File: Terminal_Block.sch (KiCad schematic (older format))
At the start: 0 parts

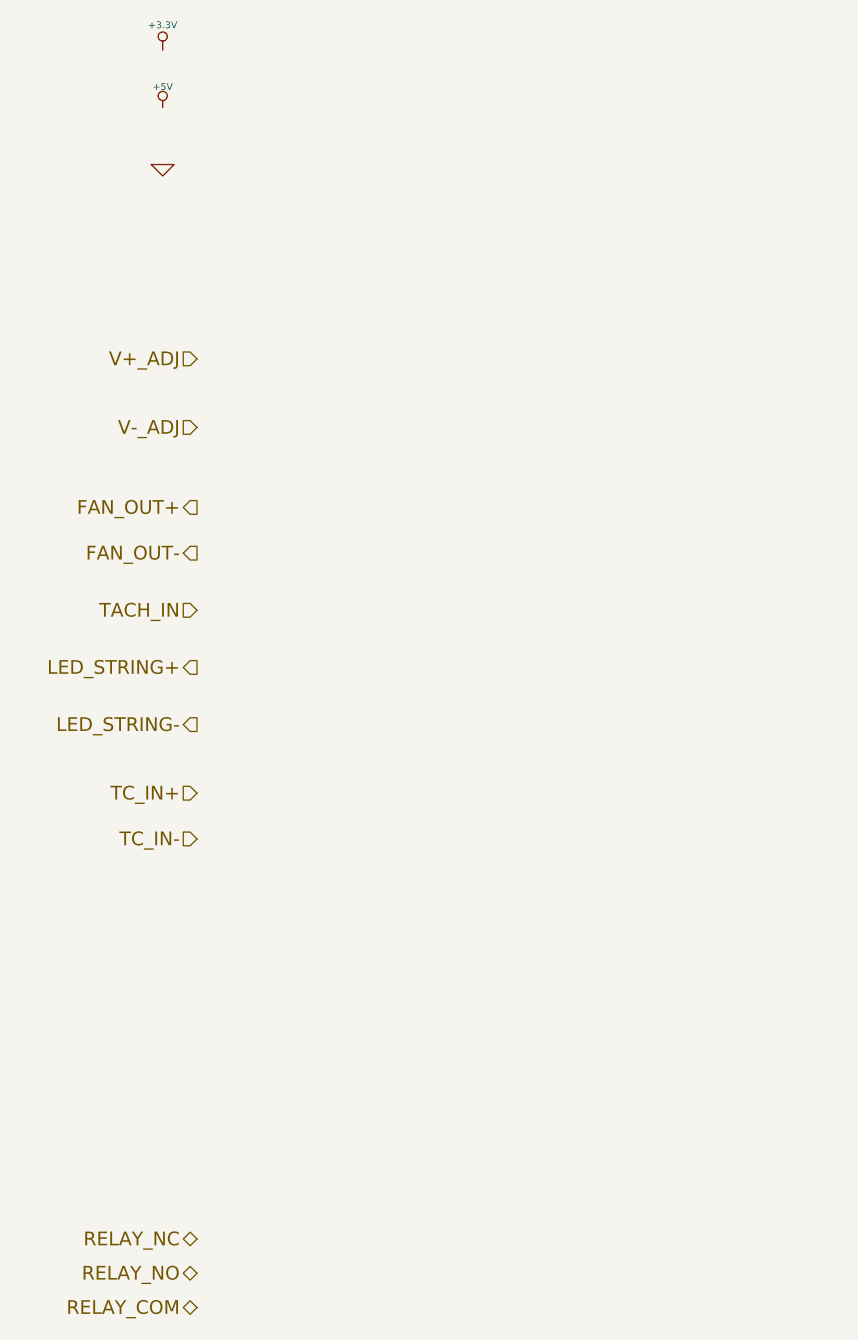
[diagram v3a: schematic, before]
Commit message: Added Arduino Connect Pin Layout
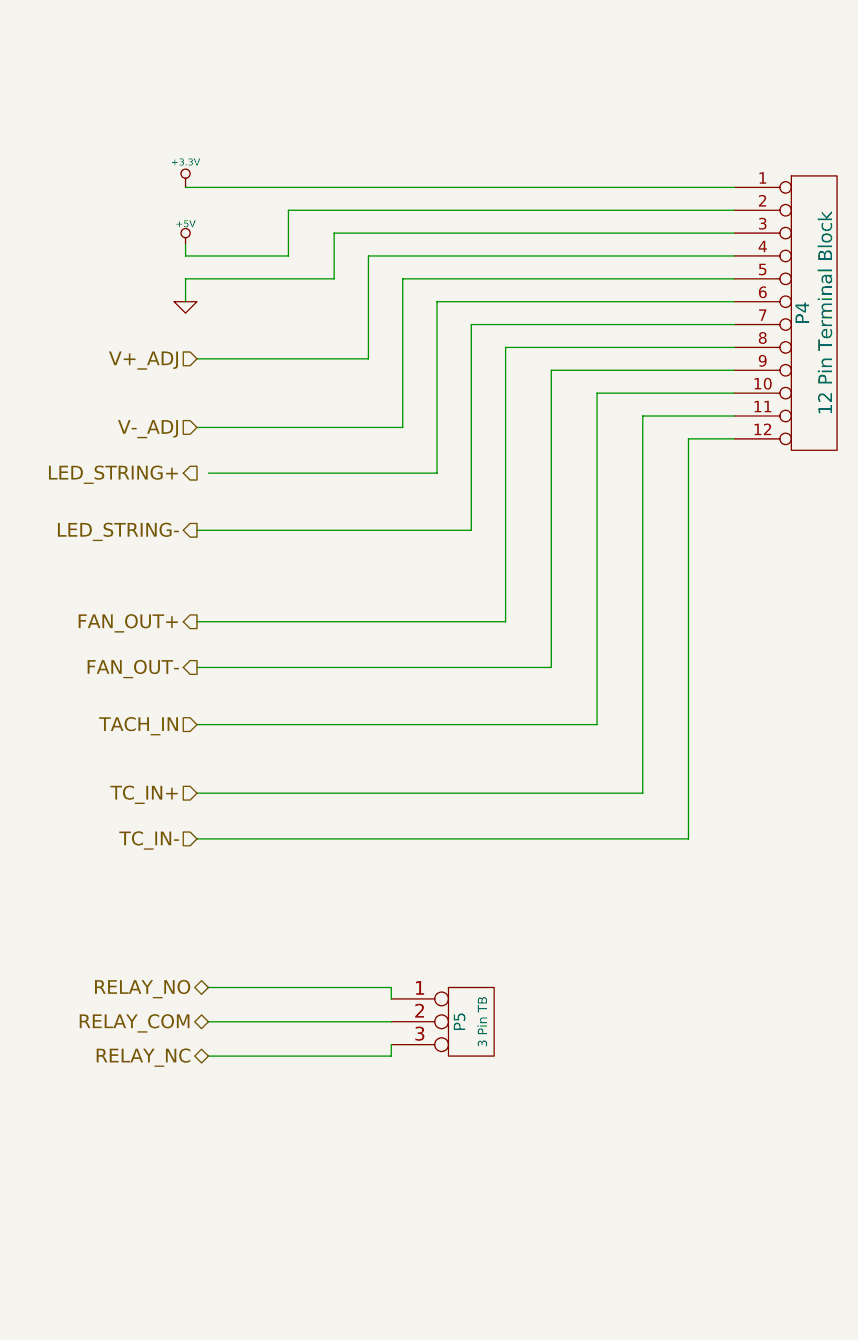
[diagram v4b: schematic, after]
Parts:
- added P4: 12 Pin Terminal Block, symbol CONN_12
- added P5: 3 Pin TB, symbol CONN_3
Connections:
- net +3.3V: now also P4.1 (P1)
- net +5V: now also P4.2 (P2)
- net FAN_OUT+: now also P4.8 (P8)
- net FAN_OUT-: now also P4.9 (P9)
- net GND: now also P4.3 (P3)
- net LED_STRING-: now also P4.7 (P7)
- net RELAY_COM: now also P5.2 (PM)
- net RELAY_NC: now also P5.3 (P3)
- net RELAY_NO: now also P5.1 (P1)
- net TACH_IN: now also P4.10 (P10)
- net TC_IN+: now also P4.11 (P11)
- net TC_IN-: now also P4.12 (P12)
- net V+_ADJ: now also P4.4 (P4)
- net V-_ADJ: now also P4.5 (P5)
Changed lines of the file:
@@
 Text HLabel 1350 2350 0    60   Input ~ 0
 V-_ADJ
-Text HLabel 1350 2700 0    60   Output ~ 0
+Text HLabel 1350 3200 0    60   Output ~ 0
 FAN_OUT+
-Text HLabel 1350 2900 0    60   Output ~ 0
+Text HLabel 1350 3400 0    60   Output ~ 0
 FAN_OUT-
-Text HLabel 1350 3150 0    60   Input ~ 0
+Text HLabel 1350 3650 0    60   Input ~ 0
 TACH_IN
-Text HLabel 1350 3400 0    60   Output ~ 0
+Text HLabel 1350 2550 0    60   Output ~ 0
 LED_STRING+
-Text HLabel 1350 3650 0    60   Output ~ 0
+Text HLabel 1350 2800 0    60   Output ~ 0
 LED_STRING-
 Text HLabel 1350 3950 0    60   Input ~ 0
@@
 Text HLabel 1350 4150 0    60   Input ~ 0
 TC_IN-
-Text HLabel 1350 5900 0    60   BiDi ~ 0
+Text HLabel 1400 5100 0    60   BiDi ~ 0
 RELAY_NC
-Text HLabel 1350 6050 0    60   BiDi ~ 0
+Text HLabel 1400 4800 0    60   BiDi ~ 0
 RELAY_NO
-Text HLabel 1350 6200 0    60   BiDi ~ 0
+Text HLabel 1400 4950 0    60   BiDi ~ 0
 RELAY_COM
 $Comp
-L +3.3V #PWR9001
+L +3.3V #PWR59
 U 1 1 52F31271
-P 1200 700
-F 0 "#PWR9001" H 1200 660 30  0001 C CNN
-F 1 "+3.3V" H 1200 810 30  0000 C CNN
-F 2 "" H 1200 700 60  0000 C CNN
-F 3 "" H 1200 700 60  0000 C CNN
-	1    1200 700
+P 1300 1300
+F 0 "#PWR59" H 1300 1260 30  0001 C CNN
+F 1 "+3.3V" H 1300 1410 30  0000 C CNN
+F 2 "" H 1300 1300 60  0000 C CNN
+F 3 "" H 1300 1300 60  0000 C CNN
+	1    1300 1300
 	1    0    0    -1
 $EndComp
 $Comp
-L +5V #PWR9002
+L +5V #PWR60
 U 1 1 52F31294
-P 1200 950
-F 0 "#PWR9002" H 1200 1040 20  0001 C CNN
-F 1 "+5V" H 1200 1040 30  0000 C CNN
-F 2 "" H 1200 950 60  0000 C CNN
-F 3 "" H 1200 950 60  0000 C CNN
-	1    1200 950
+P 1300 1550
+F 0 "#PWR60" H 1300 1640 20  0001 C CNN
+F 1 "+5V" H 1300 1640 30  0000 C CNN
+F 2 "" H 1300 1550 60  0000 C CNN
+F 3 "" H 1300 1550 60  0000 C CNN
+	1    1300 1550
 	1    0    0    -1
 $EndComp
 $Comp
-L GND #PWR9003
+L GND #PWR61
 U 1 1 52F312A3
-P 1200 1200
-F 0 "#PWR9003" H 1200 1200 30  0001 C CNN
-F 1 "GND" H 1200 1130 30  0001 C CNN
-F 2 "" H 1200 1200 60  0000 C CNN
-F 3 "" H 1200 1200 60  0000 C CNN
-	1    1200 1200
+P 1300 1800
+F 0 "#PWR61" H 1300 1800 30  0001 C CNN
+F 1 "GND" H 1300 1730 30  0001 C CNN
+F 2 "" H 1300 1800 60  0000 C CNN
+F 3 "" H 1300 1800 60  0000 C CNN
+	1    1300 1800
 	1    0    0    -1
 $EndComp
+$Comp
+L CONN_12 P4
+U 1 1 53033C28
+P 4050 1850
+F 0 "P4" V 4000 1850 60  0000 C CNN
+F 1 "12 Pin Terminal Block" V 4100 1850 60  0000 C CNN
+F 2 "" H 4050 1850 60  0000 C CNN
+F 3 "" H 4050 1850 60  0000 C CNN
+F 4 "On Shore" H 4050 1850 60  0001 C CNN "MFG Name"
+F 5 "OSTTE120104" H 4050 1850 60  0001 C CNN "MFG Part Number"
+	1    4050 1850
+	1    0    0    -1
+$EndComp
+Wire Wire Line
+	1300 1300 3700 1300
+Wire Wire Line
+	3700 1400 1750 1400
+Wire Wire Line
+	1750 1400 1750 1600
+Wire Wire Line
+	1750 1600 1300 1600
+Wire Wire Line
+	1300 1600 1300 1550
+Wire Wire Line
+	1300 1800 1300 1700
+Wire Wire Line
+	1300 1700 1950 1700
+Wire Wire Line
+	1950 1700 1950 1500
+Wire Wire Line
+	1950 1500 3700 1500
+Wire Wire Line
+	1350 2050 2100 2050
+Wire Wire Line
+	2100 2050 2100 1600
+Wire Wire Line
+	2100 1600 3700 1600
+Wire Wire Line
+	1350 2350 2250 2350
+Wire Wire Line
+	2250 2350 2250 1700
+Wire Wire Line
+	2250 1700 3700 1700
+Wire Wire Line
+	1400 2550 2400 2550
+Wire Wire Line
+	2400 2550 2400 1800
+Wire Wire Line
+	2400 1800 3700 1800
+Wire Wire Line
+	1350 2800 2550 2800
+Wire Wire Line
+	2550 2800 2550 1900
+Wire Wire Line
+	2550 1900 3700 1900
+Wire Wire Line
+	1350 3200 2700 3200
+Wire Wire Line
+	2700 3200 2700 2000
+Wire Wire Line
+	2700 2000 3700 2000
+Wire Wire Line
+	1350 3400 2900 3400
+Wire Wire Line
+	2900 3400 2900 2100
+Wire Wire Line
+	2900 2100 3700 2100
+Wire Wire Line
+	1350 3650 3100 3650
+Wire Wire Line
+	3100 3650 3100 2200
+Wire Wire Line
+	3100 2200 3700 2200
+Wire Wire Line
+	1350 3950 3300 3950
+Wire Wire Line
+	3300 3950 3300 2300
+Wire Wire Line
+	3300 2300 3700 2300
+Wire Wire Line
+	1350 4150 3500 4150
+Wire Wire Line
+	3500 4150 3500 2400
+Wire Wire Line
+	3500 2400 3700 2400
+$Comp
+L CONN_3 P5
+U 1 1 53033D8F
+P 2550 4950
+F 0 "P5" V 2500 4950 50  0000 C CNN
+F 1 "3 Pin TB" V 2600 4950 40  0000 C CNN
+F 2 "" H 2550 4950 60  0000 C CNN
+F 3 "" H 2550 4950 60  0000 C CNN
+F 4 "Pheonix" H 2550 4950 60  0001 C CNN "MFG Name"
+F 5 "1935174" H 2550 4950 60  0001 C CNN "MFG Part Number"
+	1    2550 4950
+	1    0    0    -1
+$EndComp
+Wire Wire Line
+	1400 4800 2200 4800
+Wire Wire Line
+	2200 4800 2200 4850
+Wire Wire Line
+	2200 4950 1400 4950
+Wire Wire Line
+	1400 5100 2200 5100
+Wire Wire Line
+	2200 5100 2200 5050
 $EndSCHEMATC
